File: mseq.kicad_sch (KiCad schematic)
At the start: 77 parts, among them J1 Screen_I2C, J3 Conn_ARM_JTAG_SWD_10, SW1 RESET, SW2 ON/OFF, SW3 MS/SLAVE, SW4 BOOT, U1 SN74AHCT125DR, U2 H11L1M, U3 MCP1703Ax-330xxTT, U4 STM32F413CHUx, U5 CP2102N-Axx-xQFN20, U6 H11L1M, Y1 32.768kHz ±20ppm 6pF, Y2 25 MHz ±20ppm 18pF

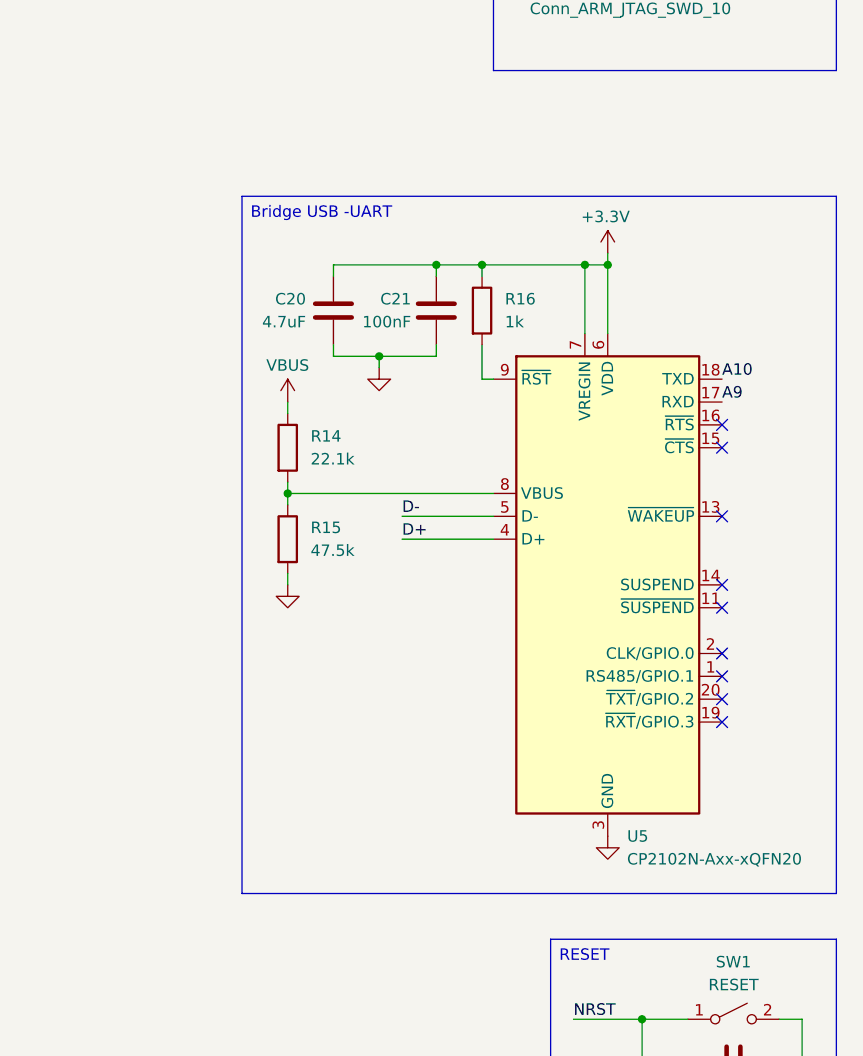
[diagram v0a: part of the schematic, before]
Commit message: LED for TXT and RXT added
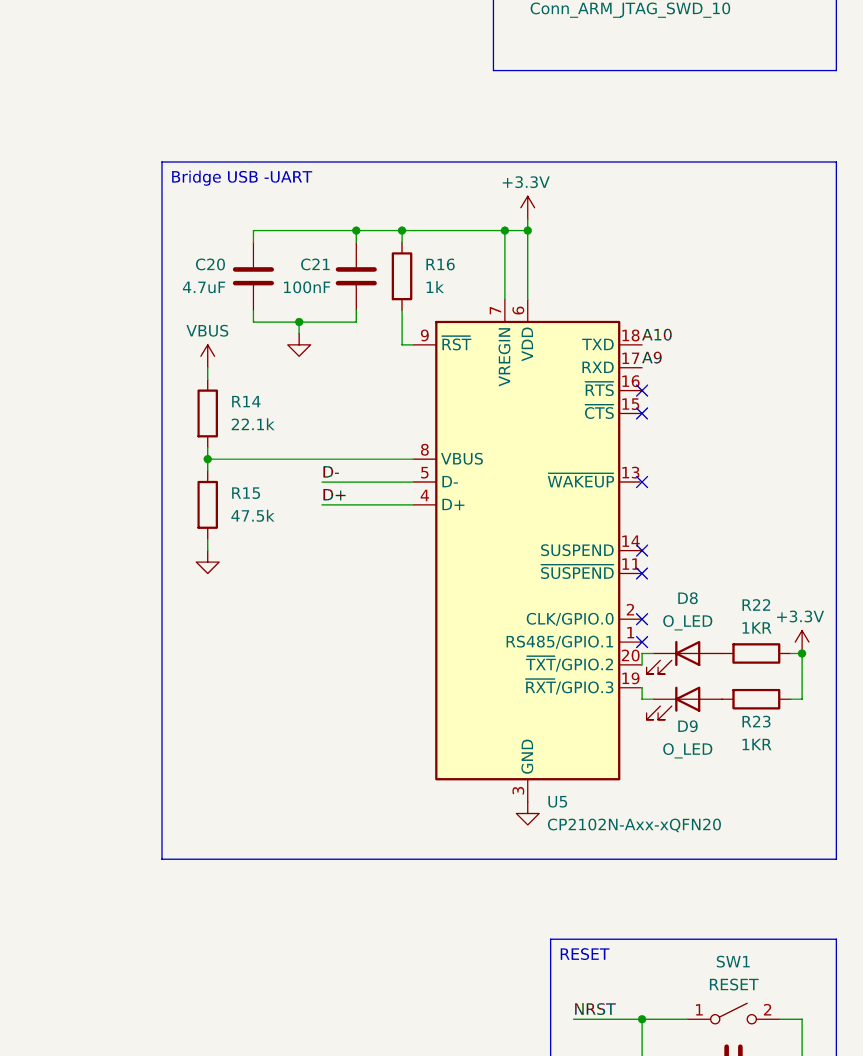
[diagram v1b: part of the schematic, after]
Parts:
- added D8, D9: O_LED, LED_SMD:LED_0603_1608Metric, symbol Device:LED
- added R22, R23: 1KR, Resistor_SMD:R_0805_2012Metric, symbol Device:R
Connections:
- net +3.3V: now also R22.1, R23.1
- net at U5.19 (~{RXT}/GPIO.3): now also D9.1 (K)
- net at U5.20 (~{TXT}/GPIO.2): now also D8.1 (K)
- new net: D9.2 (A), R23.2
- new net: D8.2 (A), R22.2
- no-connect marks 51 -> 49
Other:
- moved on the sheet: C20, C21, R14, R15, R16, U5
